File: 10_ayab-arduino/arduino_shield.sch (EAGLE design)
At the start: 22 parts, among them IC3 PCF8574T, IC4 PCF8574T

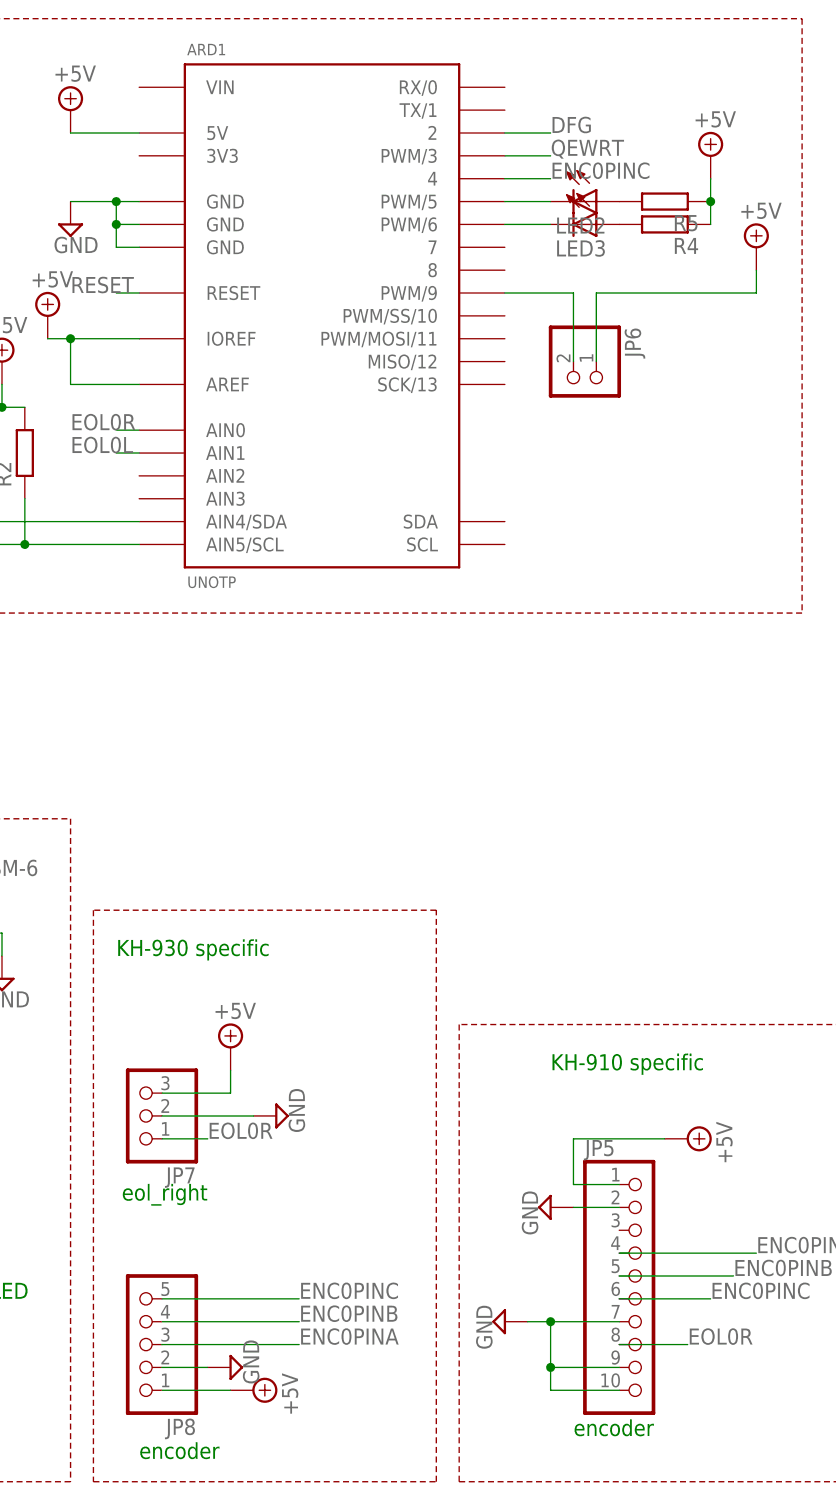
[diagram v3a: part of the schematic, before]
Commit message: added defines for KH930 fixed pinning for S3 of KH930
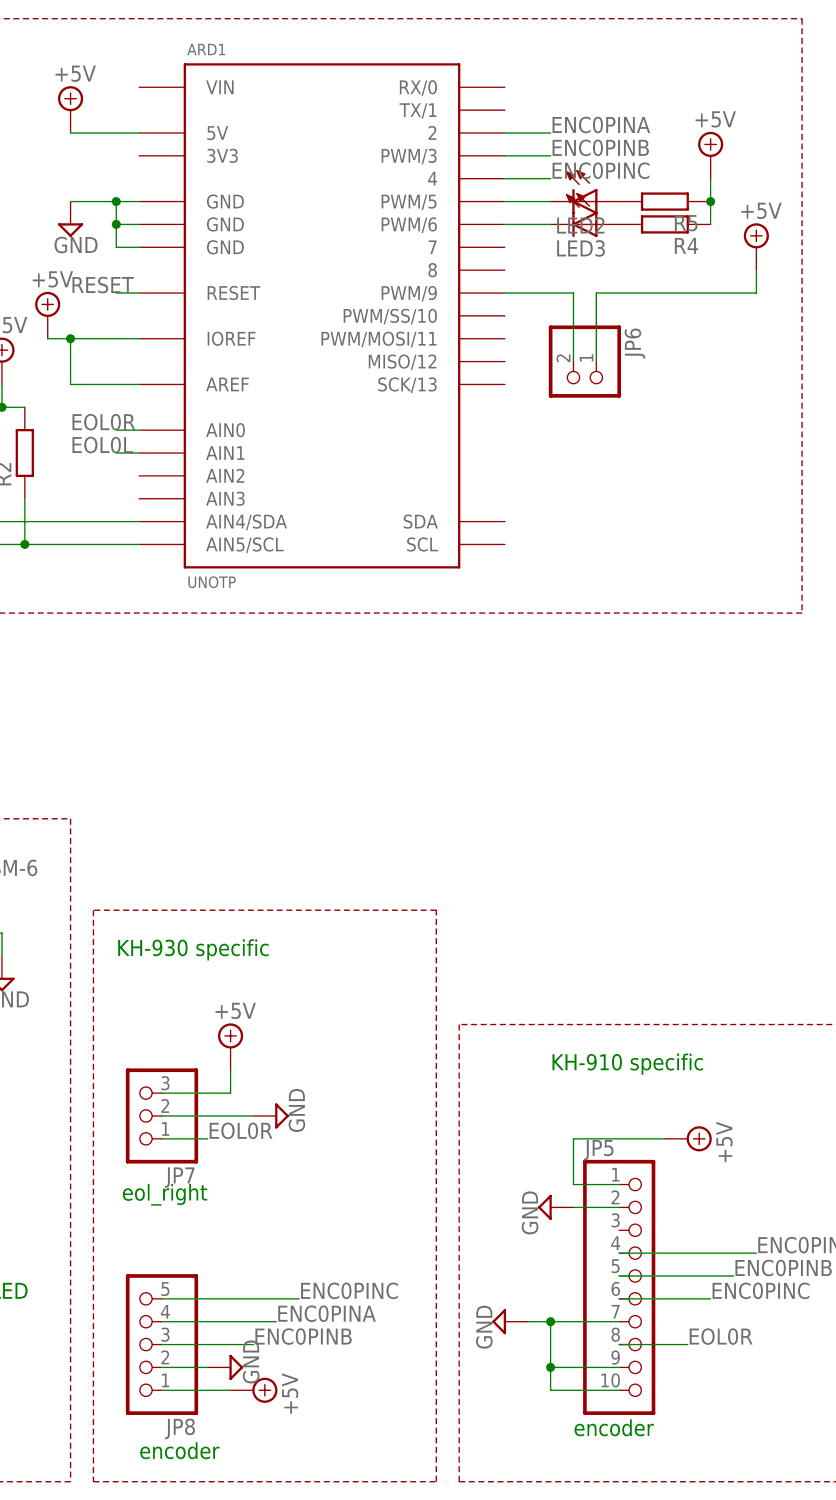
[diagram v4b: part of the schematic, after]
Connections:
- removed net DFG: ARD1.2
- removed net QEWRT: ARD1.PWM/3
- net ENC0PINA: now also ARD1.2, JP8.4; no longer JP8.3
- net ENC0PINB: now also ARD1.PWM/3, JP8.3; no longer JP8.4
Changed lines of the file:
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@@
-</segment>
-</net>
-<net name="DFG" class="0">
-<segment>
-<pinref part="ARD1" gate="G$1" pin="2"/>
-<wire x1="-48.26" y1="60.96" x2="-43.18" y2="60.96" width="0.1524" layer="91"/>
-<label x="-43.18" y="60.96" size="1.778" layer="95"/>
-</segment>
-</net>
-<net name="QEWRT" class="0">
-<segment>
-<pinref part="ARD1" gate="G$1" pin="PWM/3"/>
-<wire x1="-48.26" y1="58.42" x2="-43.18" y2="58.42" width="0.1524" layer="91"/>
-<label x="-43.18" y="58.42" size="1.778" layer="95"/>
 </segment>
 </net>
@@
 </segment>
 <segment>
-<pinref part="JP8" gate="A" pin="3"/>
-<wire x1="-86.36" y1="-73.66" x2="-71.12" y2="-73.66" width="0.1524" layer="91"/>
-<label x="-71.12" y="-73.66" size="1.778" layer="95"/>
+<pinref part="JP8" gate="A" pin="4"/>
+<wire x1="-86.36" y1="-71.12" x2="-73.66" y2="-71.12" width="0.1524" layer="91"/>
+<label x="-73.66" y="-71.12" size="1.778" layer="95"/>
+</segment>
+<segment>
+<pinref part="ARD1" gate="G$1" pin="2"/>
+<wire x1="-48.26" y1="60.96" x2="-43.18" y2="60.96" width="0.1524" layer="91"/>
+<label x="-43.18" y="60.96" size="1.778" layer="95"/>
 </segment>
 </net>
@@
 </segment>
 <segment>
-<pinref part="JP8" gate="A" pin="4"/>
-<wire x1="-86.36" y1="-71.12" x2="-71.12" y2="-71.12" width="0.1524" layer="91"/>
-<label x="-71.12" y="-71.12" size="1.778" layer="95"/>
-</segment>
-</net>
+<pinref part="JP8" gate="A" pin="3"/>
+<wire x1="-86.36" y1="-73.66" x2="-76.2" y2="-73.66" width="0.1524" layer="91"/>
+<label x="-76.2" y="-73.66" size="1.778" layer="95"/>
+</segment>
+<segment>
+<pinref part="ARD1" gate="G$1" pin="PWM/3"/>
+<wire x1="-48.26" y1="58.42" x2="-43.18" y2="58.42" width="0.1524" layer="91"/>
+<label x="-43.18" y="58.42" size="1.778" layer="95"/>
+</segment>
+</net>

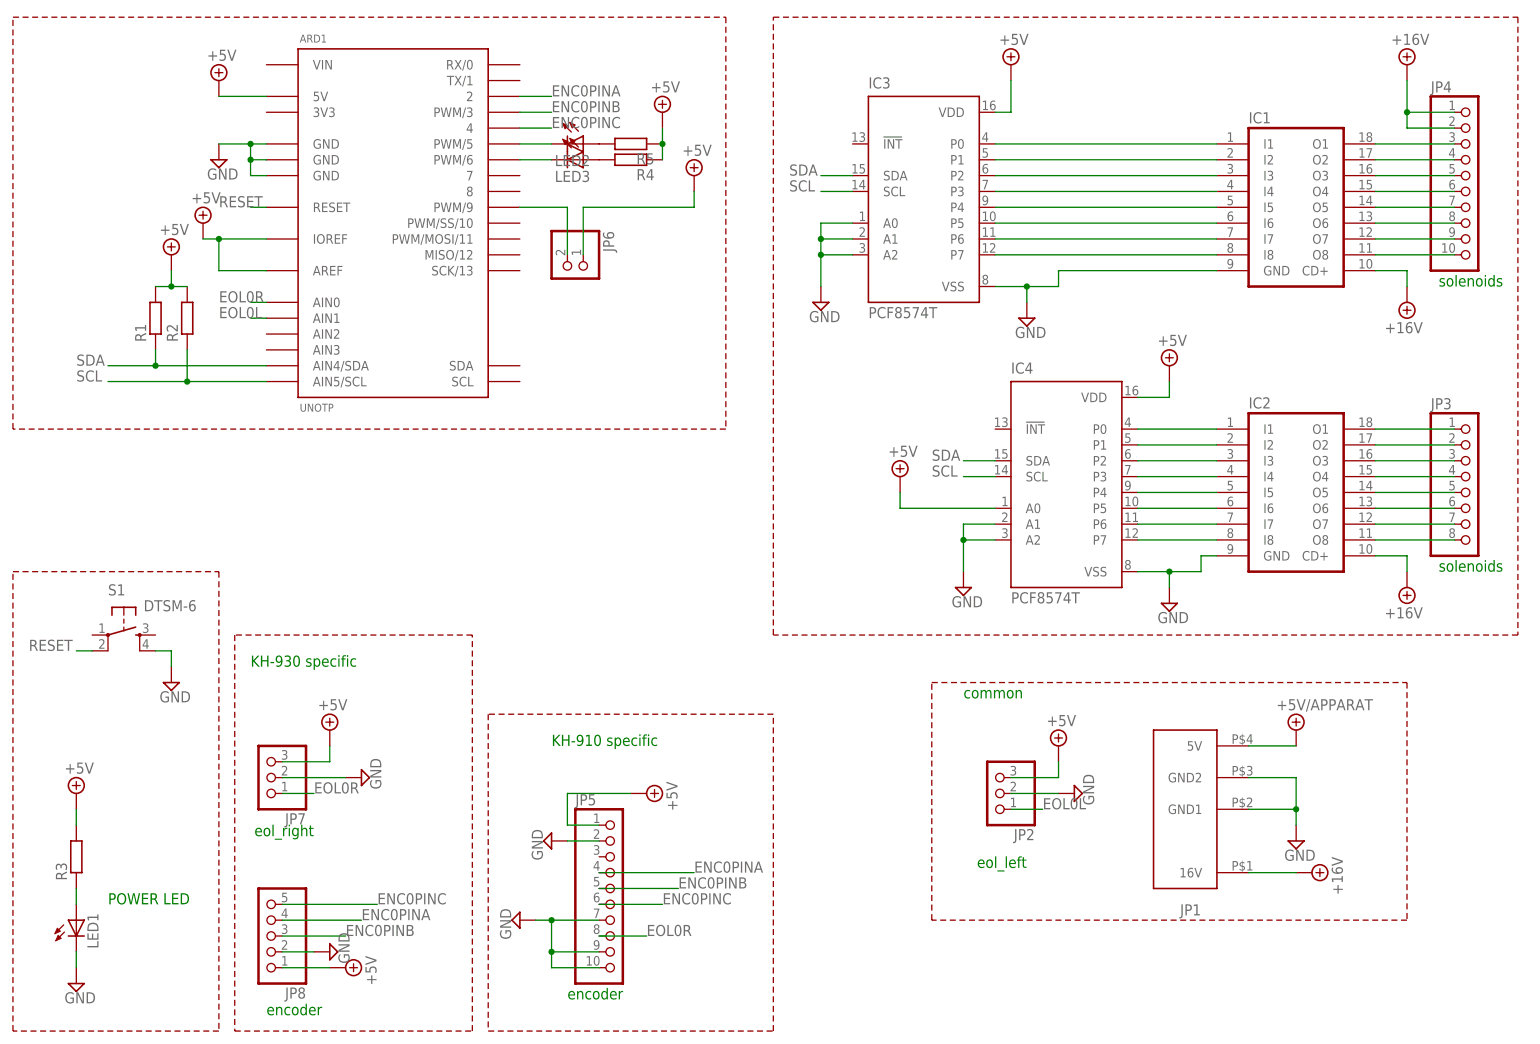
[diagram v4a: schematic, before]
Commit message: Created a shield version without SMD-Parts
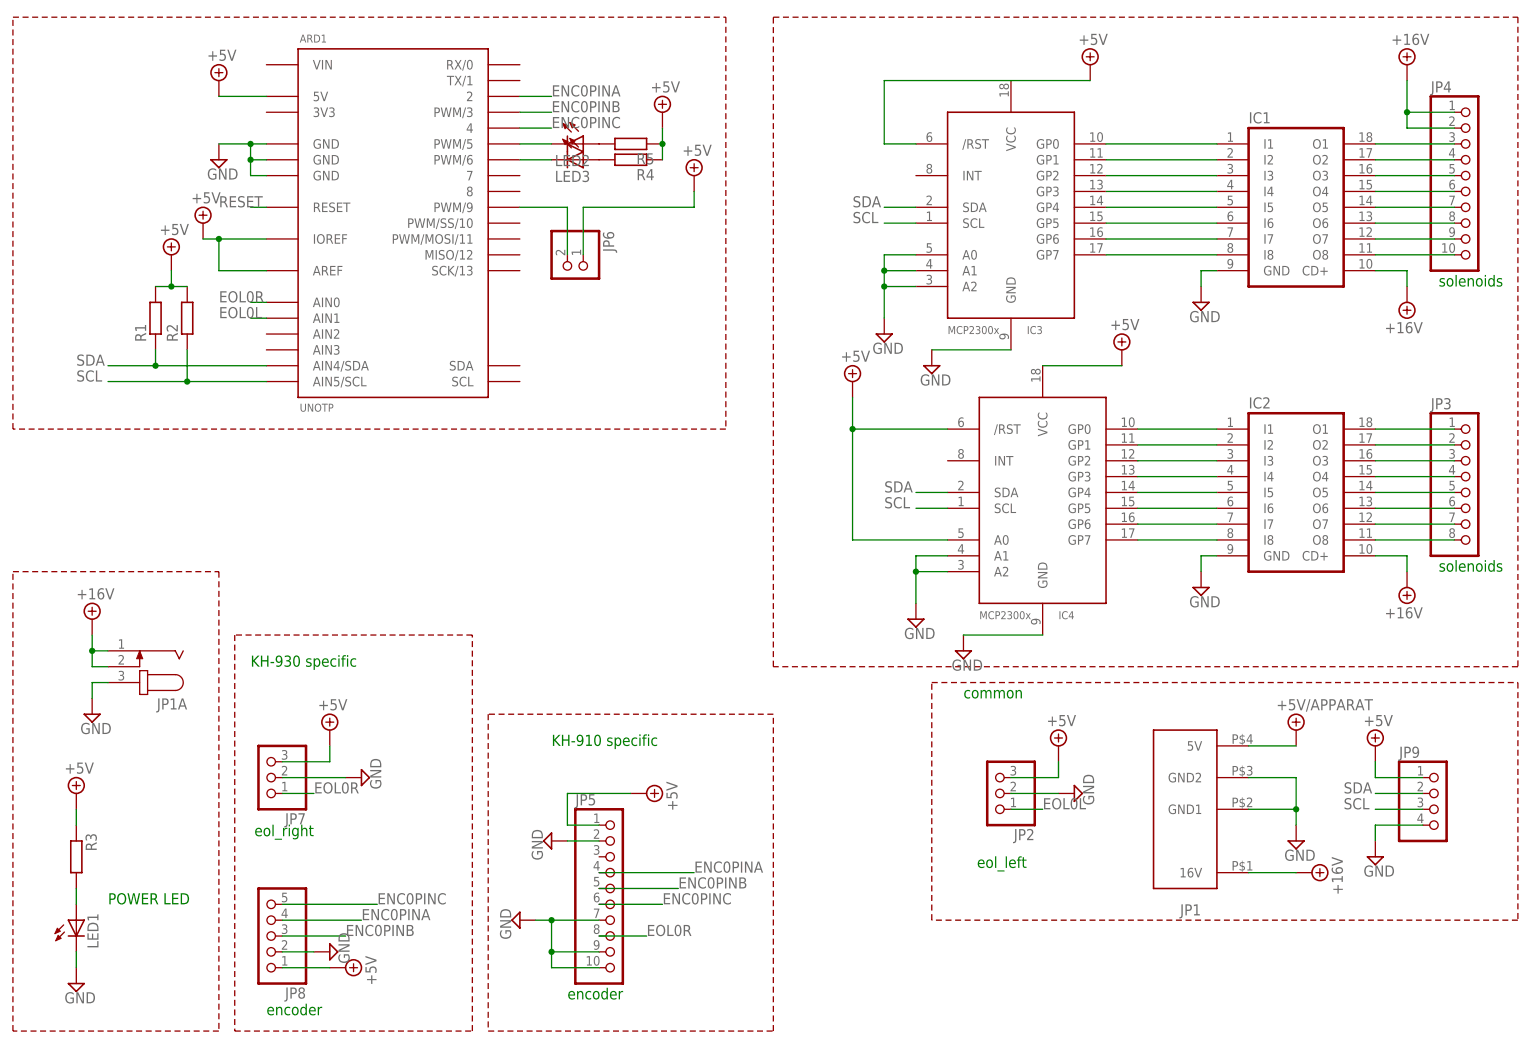
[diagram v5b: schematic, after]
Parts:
- removed S1: DTSM-6, switch-tact:DTSM-6
- added JP1A: (no value), con-jack:JACK-PLUG1
- added JP9: (no value), pinhead:PINHD-1X4
- IC3, IC4: value PCF8574T -> MCP2300X/P; device micro-philips:PCF8574T -> adafruit:MCP2300X/P
- LED1, LED2, LED3: device adafruit:LEDCHIP-LED0805 -> led:LED3MM
- R1, R2: device rcl:R-EU_R0805 -> rcl:R-EU_0207/2V
- R3, R4, R5: device resistor:R-EU_R0805 -> rcl:R-EU_0207/2V
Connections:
- net +15V: now also JP1A.1, JP1A.2
- net +5V: now also IC3./RST, IC3.VCC, IC4./RST, IC4.VCC, JP9.1, R3.1; no longer IC3.VDD, IC4.VDD, R3.2
- net GND: now also IC3.GND, IC4.GND, JP1A.3, JP9.4; no longer IC3.VSS, IC4.VSS, S1.4
- net N$1: now also IC4.GP0; no longer IC4.P0
- net N$10: now also IC4.GP1; no longer IC4.P1
- net N$11: now also IC4.GP2; no longer IC4.P2
- net N$12: now also IC4.GP3; no longer IC4.P3
- net N$13: now also IC4.GP4; no longer IC4.P4
- net N$14: now also IC4.GP5; no longer IC4.P5
- net N$15: now also IC4.GP6; no longer IC4.P6
- net N$16: now also IC4.GP7; no longer IC4.P7
- net N$2: now also IC3.GP0; no longer IC3.P0
- net N$3: now also IC3.GP1; no longer IC3.P1
- net N$33: now also R3.2; no longer R3.1
- net N$4: now also IC3.GP2; no longer IC3.P2
- net N$5: now also IC3.GP3; no longer IC3.P3
- net N$6: now also IC3.GP4; no longer IC3.P4
- net N$7: now also IC3.GP5; no longer IC3.P5
- net N$8: now also IC3.GP6; no longer IC3.P6
- net N$9: now also IC3.GP7; no longer IC3.P7
- net RESET: no longer S1.2
- net SCL: now also JP9.3
- net SDA: now also JP9.2
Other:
- moved on the sheet: R3

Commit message: Finalization of AYAB Shield 1.3 Through Hole
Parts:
- removed JP1A: (no value), con-jack:JACK-PLUG1
- added X1: NEB1R, con-lumberg:NEB1R
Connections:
- net +15V: now also X1.2, X1.3; no longer JP1A.1, JP1A.2
- net GND: now also X1.1@1; no longer JP1A.3
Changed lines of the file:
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@@
 <part name="SUPPLY34" library="supply2" deviceset="+5V" device=""/>
 <part name="SUPPLY35" library="supply2" deviceset="GND" device=""/>
-<part name="JP1A" library="con-jack" deviceset="JACK-PLUG" device="1"/>
 <part name="SUPPLY27" library="supply2" deviceset="GND" device=""/>
 <part name="SUPPLY36" library="supply2" deviceset="+15V" device="" value="+16V"/>
+<part name="X1" library="con-lumberg" deviceset="NEB1R" device=""/>
 </parts>
 <sheets>
@@
 <instance part="SUPPLY34" gate="+5V" x="88.9" y="-43.18"/>
 <instance part="SUPPLY35" gate="GND" x="88.9" y="-60.96"/>
-<instance part="JP1A" gate="G$1" x="-109.22" y="-30.48" rot="R180"/>
 <instance part="SUPPLY27" gate="GND" x="-116.84" y="-38.1"/>
 <instance part="SUPPLY36" gate="+15V" x="-116.84" y="-22.86"/>
+<instance part="X1" gate="G$1" x="-109.22" y="-30.48"/>
 </instances>
 <busses>
@@
 </segment>
 <segment>
-<pinref part="JP1A" gate="G$1" pin="3"/>
 <pinref part="SUPPLY27" gate="GND" pin="GND"/>
 <wire x1="-114.3" y1="-33.02" x2="-116.84" y2="-33.02" width="0.1524" layer="91"/>
 <wire x1="-116.84" y1="-33.02" x2="-116.84" y2="-35.56" width="0.1524" layer="91"/>
+<pinref part="X1" gate="G$1" pin="1@1"/>
 </segment>
 </net>
@@
 <pinref part="SUPPLY36" gate="+15V" pin="+15V"/>
 <wire x1="-116.84" y1="-25.4" x2="-116.84" y2="-27.94" width="0.1524" layer="91"/>
-<pinref part="JP1A" gate="G$1" pin="1"/>
 <wire x1="-116.84" y1="-27.94" x2="-114.3" y2="-27.94" width="0.1524" layer="91"/>
-<pinref part="JP1A" gate="G$1" pin="2"/>
 <wire x1="-114.3" y1="-30.48" x2="-116.84" y2="-30.48" width="0.1524" layer="91"/>
 <wire x1="-116.84" y1="-30.48" x2="-116.84" y2="-27.94" width="0.1524" layer="91"/>
 <junction x="-116.84" y="-27.94"/>
-</segment>
-</net>
+<pinref part="X1" gate="G$1" pin="3"/>
+<pinref part="X1" gate="G$1" pin="2"/>
+</segment>
+</net>
